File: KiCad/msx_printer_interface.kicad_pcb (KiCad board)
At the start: 2 copper layers, 65.7 x 54 mm, 12 parts, among them J1 MSX Cartridge Connector, J2 Conn_02x07_Top_Bottom, U1 ATF22V10C-15PU, U2 74HC273

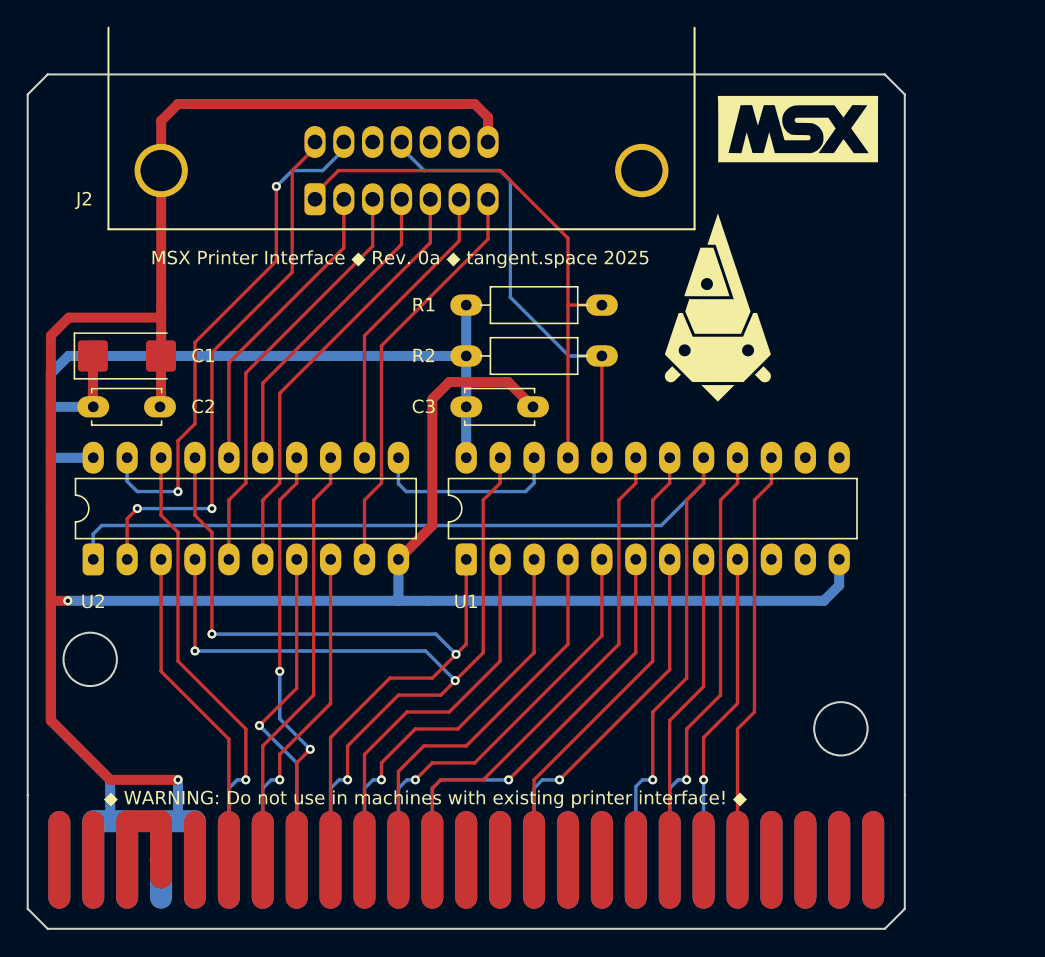
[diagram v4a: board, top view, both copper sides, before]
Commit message: Routing, silkscreen changes
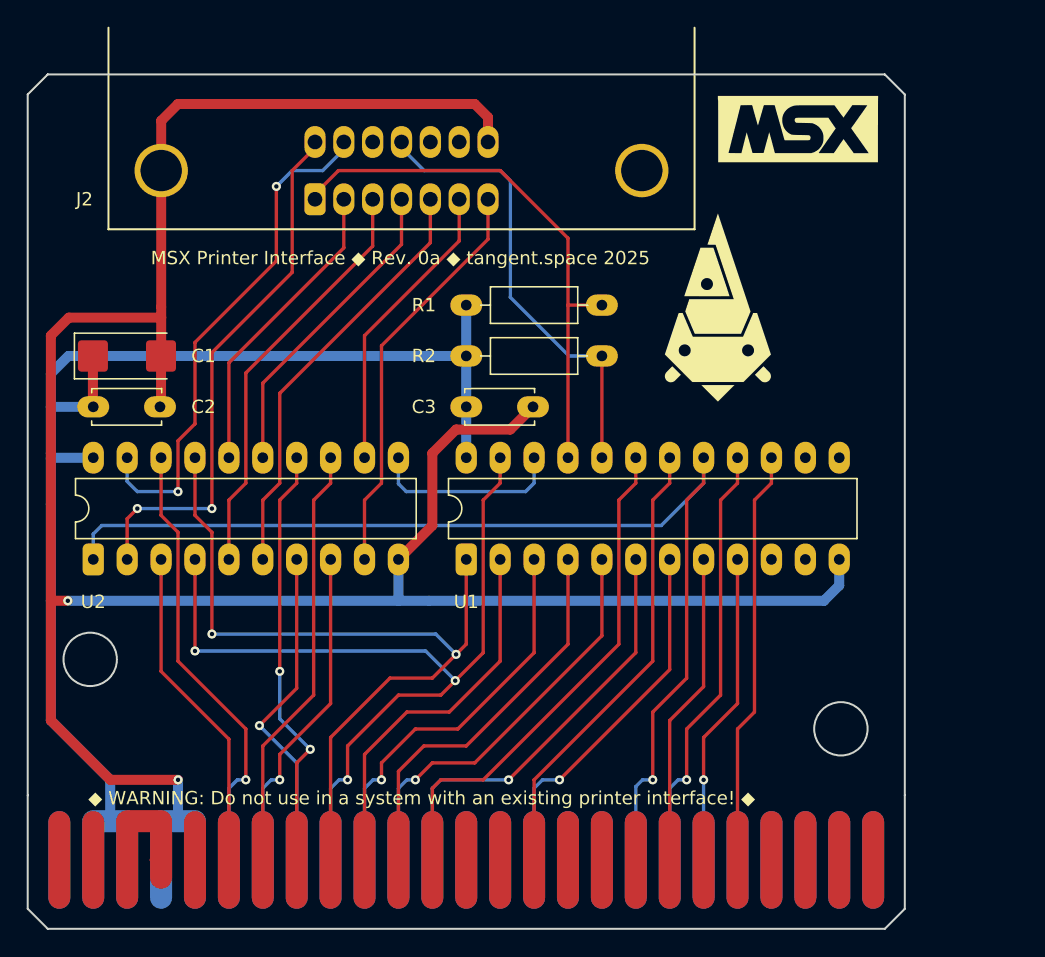
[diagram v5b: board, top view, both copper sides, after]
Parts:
- removed the G*** at (81.0, 19.1)
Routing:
- net GND: track 189.7 -> 185.8 mm
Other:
- board text added: "◆ WARNING: Do not use in a system with an existing printer interface! ◆"
- board text removed: "◆ WARNING: Do not use in machines with existing printer interface! ◆"
